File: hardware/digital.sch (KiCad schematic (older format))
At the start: 68 parts, among them J10 Conn_02x03_Counter_Clockwise, J11 Conn_02x05_Odd_Even, J12 Conn_01x03, SW1 SW_Push, SW2 SW_Push, SW3 SW_Push, U10 74LVC4245, U11 74LVC4245, U8 STM32F103V8Tx, U9 74LVC4245, Y1 12MHz

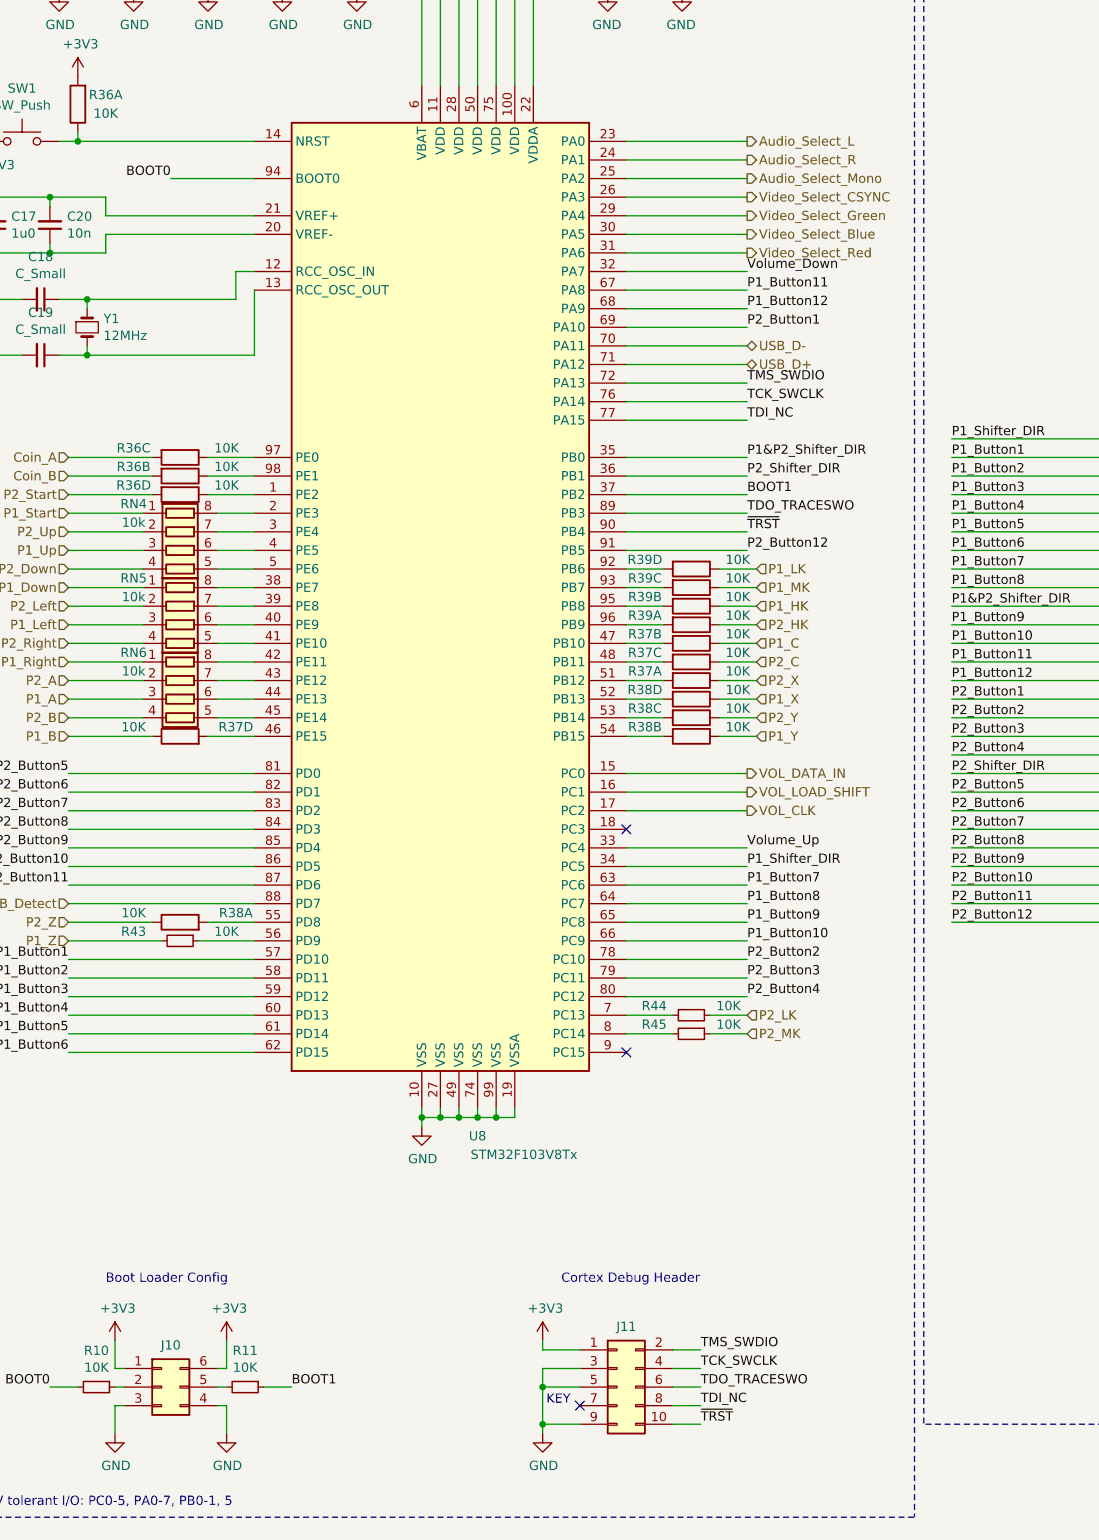
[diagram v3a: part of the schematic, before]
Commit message: Completing layout & minor edits for the main PCB. Added a project for the adapters to plug controllers into.
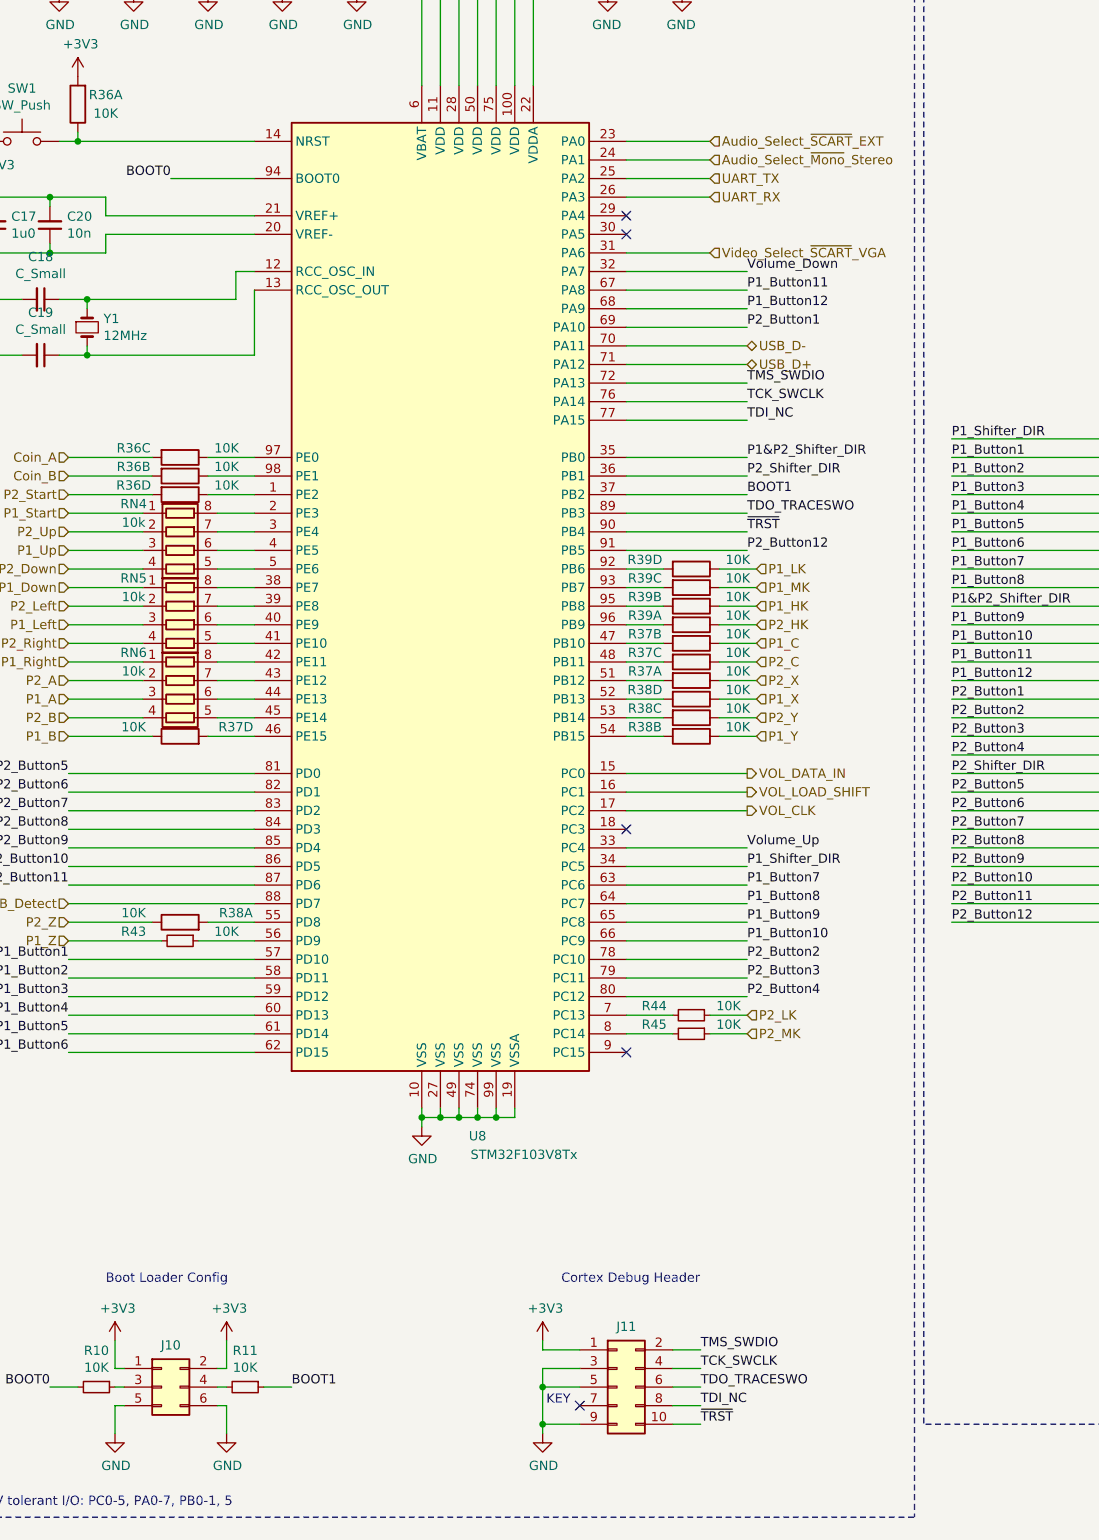
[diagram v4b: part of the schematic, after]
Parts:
- removed J10: Conn_02x03_Counter_Clockwise, Connector_PinSocket_2.54mm:PinSocket_2x03_P2.54mm_Vertical_SMD, symbol Connector_Generic:Conn_02x03_Counter_Clockwise
- added J10: Conn_02x03_Odd_Even, Connector_PinHeader_2.54mm:PinHeader_2x03_P2.54mm_Vertical_SMD, symbol Connector_Generic:Conn_02x03_Odd_Even
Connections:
- net +3V3: now also J10.1 (Pin_1), J10.2 (Pin_2)
- net GND: now also J10.5 (Pin_5), J10.6 (Pin_6)
- net at R10.1: now also J10.3 (Pin_3)
- net at R11.2: now also J10.4 (Pin_4)
- net Audio_Select_L renamed Audio_Select_~SCART~_EXT
- net Audio_Select_Mono renamed UART_TX
- net Audio_Select_R renamed Audio_Select_~Mono~_Stereo
- net Video_Select_Blue: no longer names the net of U8.30 (PA5)
- net Video_Select_CSYNC renamed UART_RX
- net Video_Select_Green: no longer names the net of U8.29 (PA4)
- net Video_Select_Red renamed Video_Select_~SCART~_VGA
- no-connect marks 3 -> 5
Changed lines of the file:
@@
 Wire Wire Line
 	800  2600 1100 2600
-$Comp
-L Connector_Generic:Conn_02x03_Counter_Clockwise J10
-U 1 1 5EB8B921
-P 1700 8700
-F 0 "J10" H 1750 8925 50  0000 C CNN
-F 1 "Conn_02x03_Counter_Clockwise" H 1750 8926 50  0001 C CNN
-F 2 "Connector_PinSocket_2.54mm:PinSocket_2x03_P2.54mm_Vertical_SMD" H 1700 8700 50  0001 C CNN
-F 3 "~" H 1700 8700 50  0001 C CNN
-	1    1700 8700
-	1    0    0    -1
-$EndComp
 Wire Wire Line
 	1500 8600 1450 8600
@@
 	4200 2700 4850 2700
 Wire Wire Line
-	4200 2600 4850 2600
-Wire Wire Line
-	4200 2500 4850 2500
-Wire Wire Line
-	4200 2400 4850 2400
+	4200 2600 4650 2600
+Wire Wire Line
+	4200 2100 4650 2100
+Wire Wire Line
+	4200 2000 4650 2000
 Text Label 4850 6100 0    50   ~ 0
 P1_Button8
@@
 P1_Button4
 Wire Wire Line
-	4200 2300 4850 2300
-Wire Wire Line
-	4200 2200 4850 2200
+	4200 2300 4650 2300
+Wire Wire Line
+	4200 2200 4650 2200
 Text Label 1200 6600 2    50   ~ 0
 P1_Button3
 Text Label 1200 6500 2    50   ~ 0
 P1_Button2
-Wire Wire Line
-	4200 2100 4850 2100
 Text Label 1200 6400 2    50   ~ 0
 P1_Button1
@@
 Text Label 4850 6200 0    50   ~ 0
 P1_Button9
-Wire Wire Line
-	4200 2000 4850 2000
 Text Label 4850 5900 0    50   ~ 0
 P1_Shifter_DIR
@@
 Text HLabel 4850 5400 2    50   Output ~ 0
 VOL_DATA_IN
-Text HLabel 4850 2000 2    50   Output ~ 0
-Audio_Select_L
-Text HLabel 4850 2100 2    50   Output ~ 0
-Audio_Select_R
-Text HLabel 4850 2200 2    50   Output ~ 0
-Audio_Select_Mono
 $Comp
 L MCU_ST_STM32F1:STM32F103V8Tx U8
@@
 	1    0    0    -1
 $EndComp
-Text HLabel 4850 2600 2    50   Output ~ 0
-Video_Select_Red
-Text HLabel 4850 2400 2    50   Output ~ 0
-Video_Select_Green
-Text HLabel 4850 2500 2    50   Output ~ 0
-Video_Select_Blue
-Text HLabel 4850 2300 2    50   Output ~ 0
-Video_Select_CSYNC
 Wire Wire Line
 	4200 5800 4850 5800
@@
 Wire Wire Line
 	4650 6800 4850 6800
+Text HLabel 4650 2600 2    50   Input ~ 0
+Video_Select_~SCART~_VGA
+Text HLabel 4650 2000 2    50   Input ~ 0
+Audio_Select_~SCART~_EXT
+Text HLabel 4650 2200 2    50   Input ~ 0
+UART_TX
+Text HLabel 4650 2300 2    50   Input ~ 0
+UART_RX
+Text HLabel 4650 2100 2    50   Input ~ 0
+Audio_Select_~Mono~_Stereo
+NoConn ~ 4200 2400
+NoConn ~ 4200 2500
+$Comp
+L Connector_Generic:Conn_02x03_Odd_Even J10
+U 1 1 5EAD6B12
+P 1700 8700
+F 0 "J10" H 1750 8925 50  0000 C CNN
+F 1 "Conn_02x03_Odd_Even" H 1750 8926 50  0001 C CNN
+F 2 "Connector_PinHeader_2.54mm:PinHeader_2x03_P2.54mm_Vertical_SMD" H 1700 8700 50  0001 C CNN
+F 3 "~" H 1700 8700 50  0001 C CNN
+	1    1700 8700
+	1    0    0    -1
+$EndComp
 $EndSCHEMATC

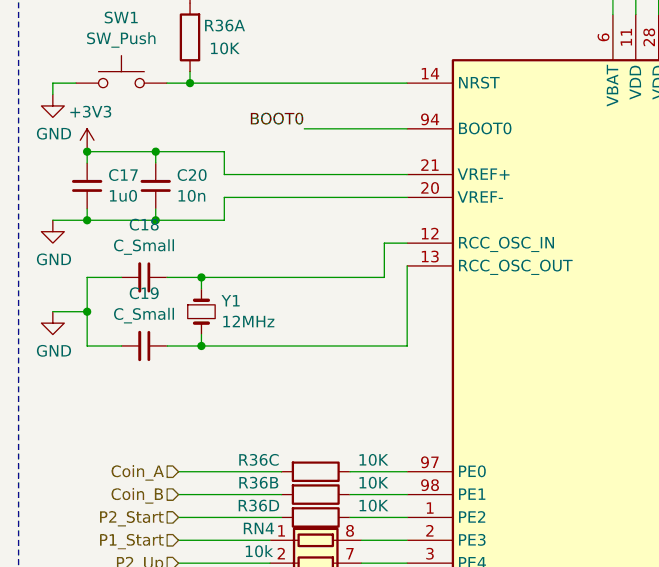
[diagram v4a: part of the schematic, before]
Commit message: Started major rework on the Audio section (chose the wrong amplifier as it can't drive 4Ohm loads) Moved over to nightly Kicad v 5.9 versions. Was a mistake to do, but will look into reverting another time.
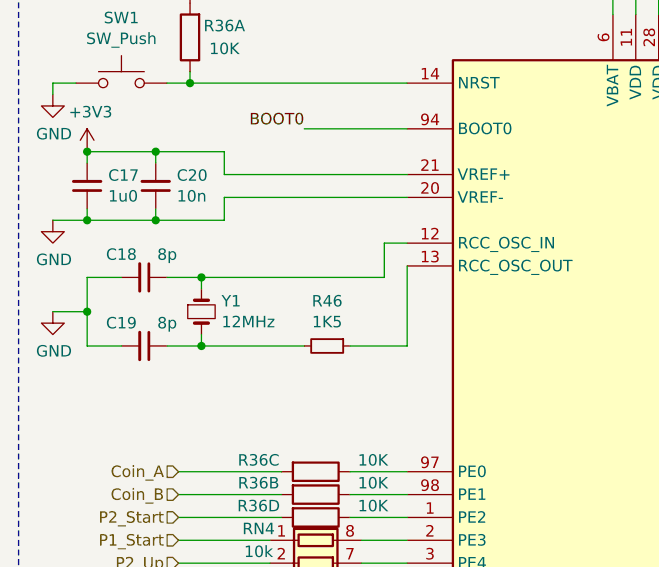
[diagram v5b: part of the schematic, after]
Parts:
- added R46: 1K5, Resistor_SMD:R_0402_1005Metric, symbol Device:R_Small
- C18, C19: value C_Small -> 8p
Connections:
- net at C19.1, Y1.2: now also R46.2; no longer U8.13 (RCC_OSC_OUT)
- new net: R46.1, U8.13 (RCC_OSC_OUT)
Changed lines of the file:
@@
 Sheet 4 4
 Title "JAMMA2Console"
-Date "2020-04-20"
-Rev "1"
+Date "2020-05-01"
+Rev "2"
 Comp "Gold"
 Comment1 ""
@@
 U 1 1 5E8DE54D
 P 1050 2850
-F 0 "C18" V 821 2850 50  0000 C CNN
-F 1 "C_Small" V 912 2850 50  0000 C CNN
+F 0 "C18" V 950 2750 50  0000 C CNN
+F 1 "8p" V 950 2950 50  0000 C CNN
 F 2 "Capacitor_SMD:C_0603_1608Metric" H 1050 2850 50  0001 C CNN
 F 3 "~" H 1050 2850 50  0001 C CNN
@@
 U 1 1 5E8DF096
 P 1050 3150
-F 0 "C19" V 821 3150 50  0000 C CNN
-F 1 "C_Small" V 912 3150 50  0000 C CNN
+F 0 "C19" V 950 3050 50  0000 C CNN
+F 1 "8p" V 950 3250 50  0000 C CNN
 F 2 "Capacitor_SMD:C_0603_1608Metric" H 1050 3150 50  0001 C CNN
 F 3 "~" H 1050 3150 50  0001 C CNN
@@
 	2100 2700 2200 2700
 Wire Wire Line
-	1300 3150 2200 3150
+	1300 3150 1750 3150
 $Comp
 L Device:C_Small C17
@@
 	1    0    0    -1
 $EndComp
+$Comp
+L Device:R_Small R46
+U 1 1 5EAFFA22
+P 1850 3150
+F 0 "R46" V 1654 3150 50  0000 C CNN
+F 1 "1K5" V 1745 3150 50  0000 C CNN
+F 2 "Resistor_SMD:R_0402_1005Metric" H 1850 3150 50  0001 C CNN
+F 3 "~" H 1850 3150 50  0001 C CNN
+	1    1850 3150
+	0    1    1    0
+$EndComp
+Wire Wire Line
+	1950 3150 2200 3150
 $EndSCHEMATC
